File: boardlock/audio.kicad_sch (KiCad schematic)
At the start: 7 parts, among them U4 MAX98357AETE+T

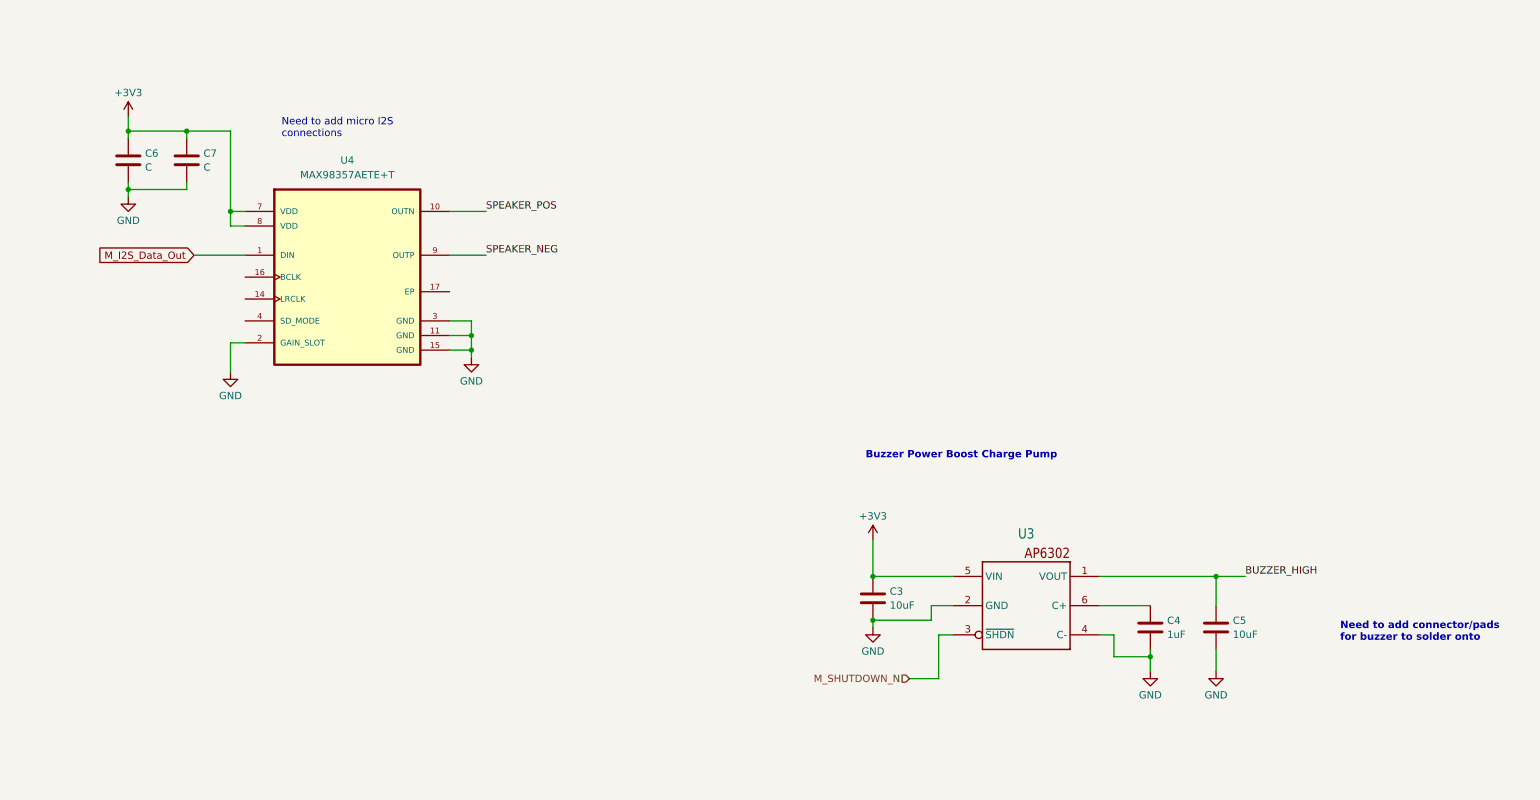
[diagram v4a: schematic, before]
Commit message: added buck boost topology
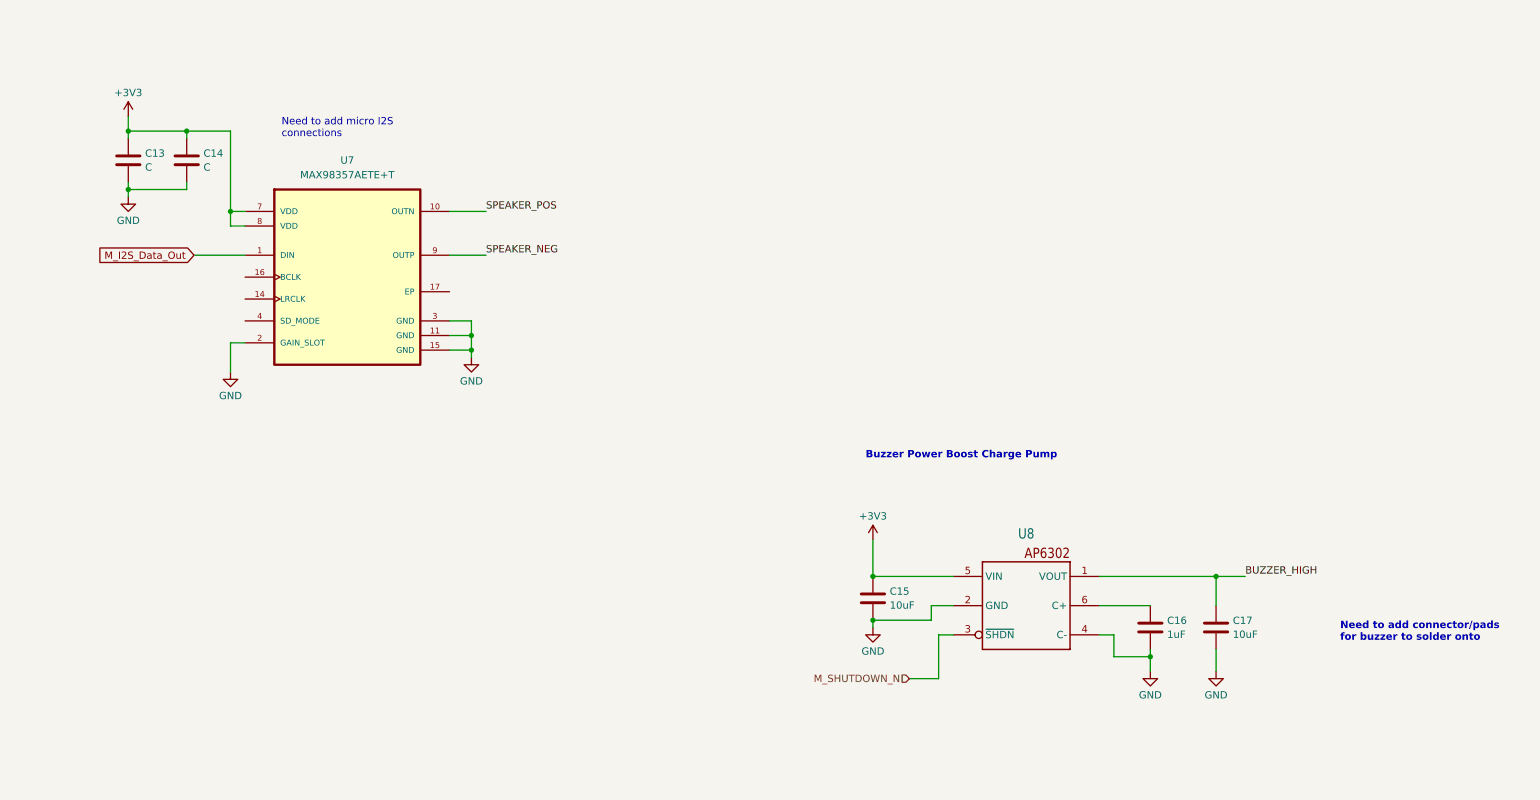
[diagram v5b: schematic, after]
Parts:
- renumbered C6 to C13, C7 to C14, C3 to C15, C4 to C16, C5 to C17, U4 to U7, U3 to U8
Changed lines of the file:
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@@
   (symbol (lib_id "Device:C") (at 231.14 125.73 0) (unit 1)
     (in_bom yes) (on_board yes) (dnp no) (fields_autoplaced)
-    (property "Reference" "C5" (at 234.061 124.5179 0)
+    (property "Reference" "C17" (at 234.061 124.5179 0)
       (effects (font (size 1.27 1.27)) (justify left))
     )
@@
       (project "boardlock"
         (path "/e1fc29ce-837e-4062-84d8-c7e423f9eab9/1eb676fb-9e7a-4e01-ba1e-2eff94d7b66e"
-          (reference "C5") (unit 1)
+          (reference "C17") (unit 1)
         )
       )
@@
   (symbol (lib_id "power:GND") (at 171.45 125.73 0) (unit 1)
     (in_bom yes) (on_board yes) (dnp no) (fields_autoplaced)
-    (property "Reference" "#PWR010" (at 171.45 132.08 0)
+    (property "Reference" "#PWR025" (at 171.45 132.08 0)
       (effects (font (size 1.27 1.27)) hide)
     )
@@
       (project "boardlock"
         (path "/e1fc29ce-837e-4062-84d8-c7e423f9eab9/1eb676fb-9e7a-4e01-ba1e-2eff94d7b66e"
-          (reference "#PWR010") (unit 1)
+          (reference "#PWR025") (unit 1)
         )
       )
@@
   (symbol (lib_id "power:GND") (at 231.14 133.35 0) (unit 1)
     (in_bom yes) (on_board yes) (dnp no) (fields_autoplaced)
-    (property "Reference" "#PWR013" (at 231.14 139.7 0)
+    (property "Reference" "#PWR027" (at 231.14 139.7 0)
       (effects (font (size 1.27 1.27)) hide)
     )
@@
       (project "boardlock"
         (path "/e1fc29ce-837e-4062-84d8-c7e423f9eab9/1eb676fb-9e7a-4e01-ba1e-2eff94d7b66e"
-          (reference "#PWR013") (unit 1)
+          (reference "#PWR027") (unit 1)
         )
       )
@@
   (symbol (lib_id "Device:C") (at 41.91 44.45 0) (unit 1)
     (in_bom yes) (on_board yes) (dnp no) (fields_autoplaced)
-    (property "Reference" "C6" (at 44.831 43.2379 0)
+    (property "Reference" "C13" (at 44.831 43.2379 0)
       (effects (font (size 1.27 1.27)) (justify left))
     )
@@
       (project "boardlock"
         (path "/e1fc29ce-837e-4062-84d8-c7e423f9eab9/1eb676fb-9e7a-4e01-ba1e-2eff94d7b66e"
-          (reference "C6") (unit 1)
+          (reference "C13") (unit 1)
         )
       )
@@
   (symbol (lib_id "Device:C") (at 171.45 120.65 0) (unit 1)
     (in_bom yes) (on_board yes) (dnp no) (fields_autoplaced)
-    (property "Reference" "C3" (at 174.371 119.4379 0)
+    (property "Reference" "C15" (at 174.371 119.4379 0)
       (effects (font (size 1.27 1.27)) (justify left))
     )
@@
       (project "boardlock"
         (path "/e1fc29ce-837e-4062-84d8-c7e423f9eab9/1eb676fb-9e7a-4e01-ba1e-2eff94d7b66e"
-          (reference "C3") (unit 1)
+          (reference "C15") (unit 1)
         )
       )
@@
   (symbol (lib_id "power:GND") (at 219.71 133.35 0) (unit 1)
     (in_bom yes) (on_board yes) (dnp no) (fields_autoplaced)
-    (property "Reference" "#PWR011" (at 219.71 139.7 0)
+    (property "Reference" "#PWR026" (at 219.71 139.7 0)
       (effects (font (size 1.27 1.27)) hide)
     )
@@
       (project "boardlock"
         (path "/e1fc29ce-837e-4062-84d8-c7e423f9eab9/1eb676fb-9e7a-4e01-ba1e-2eff94d7b66e"
-          (reference "#PWR011") (unit 1)
+          (reference "#PWR026") (unit 1)
         )
       )
@@
   (symbol (lib_id "power:+3V3") (at 171.45 110.49 0) (unit 1)
     (in_bom yes) (on_board yes) (dnp no) (fields_autoplaced)
-    (property "Reference" "#PWR012" (at 171.45 114.3 0)
+    (property "Reference" "#PWR024" (at 171.45 114.3 0)
       (effects (font (size 1.27 1.27)) hide)
     )
@@
       (project "boardlock"
         (path "/e1fc29ce-837e-4062-84d8-c7e423f9eab9/1eb676fb-9e7a-4e01-ba1e-2eff94d7b66e"
-          (reference "#PWR012") (unit 1)
+          (reference "#PWR024") (unit 1)
         )
       )
@@
   (symbol (lib_id "power:+3V3") (at 41.91 36.83 0) (unit 1)
     (in_bom yes) (on_board yes) (dnp no) (fields_autoplaced)
-    (property "Reference" "#PWR014" (at 41.91 40.64 0)
+    (property "Reference" "#PWR020" (at 41.91 40.64 0)
       (effects (font (size 1.27 1.27)) hide)
     )
@@
       (project "boardlock"
         (path "/e1fc29ce-837e-4062-84d8-c7e423f9eab9/1eb676fb-9e7a-4e01-ba1e-2eff94d7b66e"
-          (reference "#PWR014") (unit 1)
+          (reference "#PWR020") (unit 1)
         )
       )
@@
   (symbol (lib_id "custom_library:AP3602") (at 198.12 121.92 0) (unit 1)
     (in_bom yes) (on_board yes) (dnp no) (fields_autoplaced)
-    (property "Reference" "U3" (at 198.12 109.4182 0)
+    (property "Reference" "U8" (at 198.12 109.4182 0)
       (effects (font (size 1.778 1.5113)))
     )
@@
       (project "boardlock"
         (path "/e1fc29ce-837e-4062-84d8-c7e423f9eab9/1eb676fb-9e7a-4e01-ba1e-2eff94d7b66e"
-          (reference "U3") (unit 1)
+          (reference "U8") (unit 1)
         )
       )
@@
   (symbol (lib_id "Device:C") (at 219.71 125.73 0) (unit 1)
     (in_bom yes) (on_board yes) (dnp no) (fields_autoplaced)
-    (property "Reference" "C4" (at 222.631 124.5179 0)
+    (property "Reference" "C16" (at 222.631 124.5179 0)
       (effects (font (size 1.27 1.27)) (justify left))
     )
@@
       (project "boardlock"
         (path "/e1fc29ce-837e-4062-84d8-c7e423f9eab9/1eb676fb-9e7a-4e01-ba1e-2eff94d7b66e"
-          (reference "C4") (unit 1)
+          (reference "C16") (unit 1)
         )
       )
@@
   (symbol (lib_id "power:GND") (at 101.6 78.74 0) (unit 1)
     (in_bom yes) (on_board yes) (dnp no) (fields_autoplaced)
-    (property "Reference" "#PWR017" (at 101.6 85.09 0)
+    (property "Reference" "#PWR023" (at 101.6 85.09 0)
       (effects (font (size 1.27 1.27)) hide)
     )
@@
       (project "boardlock"
         (path "/e1fc29ce-837e-4062-84d8-c7e423f9eab9/1eb676fb-9e7a-4e01-ba1e-2eff94d7b66e"
-          (reference "#PWR017") (unit 1)
+          (reference "#PWR023") (unit 1)
         )
       )
@@
   (symbol (lib_id "power:GND") (at 41.91 50.8 0) (unit 1)
     (in_bom yes) (on_board yes) (dnp no) (fields_autoplaced)
-    (property "Reference" "#PWR015" (at 41.91 57.15 0)
+    (property "Reference" "#PWR021" (at 41.91 57.15 0)
       (effects (font (size 1.27 1.27)) hide)
     )
@@
       (project "boardlock"
         (path "/e1fc29ce-837e-4062-84d8-c7e423f9eab9/1eb676fb-9e7a-4e01-ba1e-2eff94d7b66e"
-          (reference "#PWR015") (unit 1)
+          (reference "#PWR021") (unit 1)
         )
       )
@@
   (symbol (lib_id "Device:C") (at 52.07 44.45 0) (unit 1)
     (in_bom yes) (on_board yes) (dnp no) (fields_autoplaced)
-    (property "Reference" "C7" (at 54.991 43.2379 0)
+    (property "Reference" "C14" (at 54.991 43.2379 0)
       (effects (font (size 1.27 1.27)) (justify left))
     )
@@
       (project "boardlock"
         (path "/e1fc29ce-837e-4062-84d8-c7e423f9eab9/1eb676fb-9e7a-4e01-ba1e-2eff94d7b66e"
-          (reference "C7") (unit 1)
+          (reference "C14") (unit 1)
         )
       )
@@
   (symbol (lib_id "MAX98357AETE+T:MAX98357AETE+T") (at 80.01 64.77 0) (unit 1)
     (in_bom yes) (on_board yes) (dnp no) (fields_autoplaced)
-    (property "Reference" "U4" (at 80.01 44.45 0)
+    (property "Reference" "U7" (at 80.01 44.45 0)
       (effects (font (size 1.27 1.27)))
     )
@@
       (project "boardlock"
         (path "/e1fc29ce-837e-4062-84d8-c7e423f9eab9/1eb676fb-9e7a-4e01-ba1e-2eff94d7b66e"
-          (reference "U4") (unit 1)
+          (reference "U7") (unit 1)
         )
       )
@@
   (symbol (lib_id "power:GND") (at 59.69 81.28 0) (unit 1)
     (in_bom yes) (on_board yes) (dnp no) (fields_autoplaced)
-    (property "Reference" "#PWR016" (at 59.69 87.63 0)
+    (property "Reference" "#PWR022" (at 59.69 87.63 0)
       (effects (font (size 1.27 1.27)) hide)
     )
@@
       (project "boardlock"
         (path "/e1fc29ce-837e-4062-84d8-c7e423f9eab9/1eb676fb-9e7a-4e01-ba1e-2eff94d7b66e"
-          (reference "#PWR016") (unit 1)
-        )
-      )
+          (reference "#PWR022") (unit 1)
+        )
+      )

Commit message: modifications?
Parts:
- added J3: Micro_SD_Card_Det1, symbol Connector:Micro_SD_Card_Det1
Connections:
- net +3V3: now also J3.4 (VDD)
- net GND: now also J3.10 (SHIELD), J3.6 (VSS), J3.9 (DET)
- new net M_SPI_CLK: J3.5 (CLK)
- new net M_SPI_CS: J3.2 (DAT3/CD)
- new net M_SPI_MISO: J3.7 (DAT0)
- new net M_SPI_MOSI: J3.3 (CMD)
- no-connect marks 0 -> 2
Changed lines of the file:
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@@
   (junction (at 171.45 124.46) (diameter 0) (color 0 0 0 0)
   )
+  (junction (at 73.66 146.05) (diameter 0) (color 0 0 0 0)
+  )
   (junction (at 59.69 53.34) (diameter 0) (color 0 0 0 0)
   )
@@
   (junction (at 219.71 130.81) (diameter 0) (color 0 0 0 0)
   )
+  (no_connect (at 90.17 140.97))
+  (no_connect (at 90.17 123.19))
+  (wire (pts (xy 73.66 149.86) (xy 73.66 146.05))
+    (stroke (width 0) (type default))
+  )
   (wire (pts (xy 219.71 130.81) (xy 219.71 133.35))
     (stroke (width 0) (type default))
   )
+  (wire (pts (xy 134.62 146.05) (xy 134.62 147.32))
+    (stroke (width 0) (type default))
+  )
   (wire (pts (xy 41.91 39.37) (xy 52.07 39.37))
     (stroke (width 0) (type default))
@@
     (stroke (width 0) (type default))
   )
+  (wire (pts (xy 73.66 146.05) (xy 73.66 135.89))
+    (stroke (width 0) (type default))
+  )
   (wire (pts (xy 59.69 76.2) (xy 59.69 81.28))
     (stroke (width 0) (type default))
   )
+  (wire (pts (xy 88.9 125.73) (xy 90.17 125.73))
+    (stroke (width 0) (type default))
+  )
   (wire (pts (xy 59.69 76.2) (xy 62.23 76.2))
     (stroke (width 0) (type default))
@@
     (stroke (width 0) (type default))
   )
+  (wire (pts (xy 90.17 133.35) (xy 88.9 133.35))
+    (stroke (width 0) (type default))
+  )
   (wire (pts (xy 41.91 36.83) (xy 41.91 39.37))
     (stroke (width 0) (type default))
@@
     (stroke (width 0) (type default))
   )
+  (wire (pts (xy 73.66 146.05) (xy 90.17 146.05))
+    (stroke (width 0) (type default))
+  )
   (wire (pts (xy 181.61 121.92) (xy 185.42 121.92))
     (stroke (width 0) (type default))
@@
     (stroke (width 0) (type default))
   )
+  (wire (pts (xy 73.66 135.89) (xy 90.17 135.89))
+    (stroke (width 0) (type default))
+  )
+  (wire (pts (xy 90.17 128.27) (xy 88.9 128.27))
+    (stroke (width 0) (type default))
+  )
   (wire (pts (xy 97.79 77.47) (xy 101.6 77.47))
     (stroke (width 0) (type default))
@@
     (stroke (width 0) (type default))
   )
+  (wire (pts (xy 134.62 146.05) (xy 133.35 146.05))
+    (stroke (width 0) (type default))
+  )
   (wire (pts (xy 59.69 53.34) (xy 59.69 55.88))
     (stroke (width 0) (type default))
@@
     (stroke (width 0) (type default))
   )
+  (wire (pts (xy 90.17 138.43) (xy 88.9 138.43))
+    (stroke (width 0) (type default))
+  )
   (wire (pts (xy 219.71 130.81) (xy 219.71 129.54))
     (stroke (width 0) (type default))
@@
     (stroke (width 0) (type default))
   )
+  (wire (pts (xy 73.66 120.65) (xy 73.66 130.81))
+    (stroke (width 0) (type default))
+  )
   (wire (pts (xy 101.6 74.93) (xy 101.6 77.47))
     (stroke (width 0) (type default))
@@
   )
   (wire (pts (xy 97.79 60.96) (xy 104.14 60.96))
+    (stroke (width 0) (type default))
+  )
+  (wire (pts (xy 73.66 130.81) (xy 90.17 130.81))
     (stroke (width 0) (type default))
   )
@@
     (effects (font (size 1.27 1.27)) (justify left bottom))
   )
+  (global_label "M_SPI_CLK" (shape input) (at 88.9 133.35 180) (fields_autoplaced)
+    (effects (font (size 1.27 1.27)) (justify right))
+    (property "Intersheetrefs" "${INTERSHEET_REFS}" (at 75.9552 133.35 0)
+      (effects (font (size 1.27 1.27)) (justify right) hide)
+    )
+  )
+  (global_label "M_SPI_MISO" (shape output) (at 88.9 138.43 180) (fields_autoplaced)
+    (effects (font (size 1.27 1.27)) (justify right))
+    (property "Intersheetrefs" "${INTERSHEET_REFS}" (at 74.9271 138.43 0)
+      (effects (font (size 1.27 1.27)) (justify right) hide)
+    )
+  )
+  (global_label "M_SPI_CS" (shape input) (at 88.9 125.73 180) (fields_autoplaced)
+    (effects (font (size 1.27 1.27)) (justify right))
+    (property "Intersheetrefs" "${INTERSHEET_REFS}" (at 77.0438 125.73 0)
+      (effects (font (size 1.27 1.27)) (justify right) hide)
+    )
+  )
   (global_label "M_I2S_Data_Out" (shape input) (at 53.34 60.96 180) (fields_autoplaced)
     (effects (font (size 1.27 1.27)) (justify right))
@@
     )
   )
+  (global_label "M_SPI_MOSI" (shape input) (at 88.9 128.27 180) (fields_autoplaced)
+    (effects (font (size 1.27 1.27)) (justify right))
+    (property "Intersheetrefs" "${INTERSHEET_REFS}" (at 74.9271 128.27 0)
+      (effects (font (size 1.27 1.27)) (justify right) hide)
+    )
+  )
   (hierarchical_label "M_SHUTDOWN_N" (shape input) (at 177.8 134.62 180) (fields_autoplaced)
     (effects (font (size 1.27 1.27)) (justify right))
@@
     )
   )
+  (symbol (lib_id "Connector:Micro_SD_Card_Det1") (at 113.03 133.35 0) (unit 1)
+    (in_bom yes) (on_board yes) (dnp no) (fields_autoplaced)
+    (property "Reference" "J3" (at 113.665 113.03 0)
+      (effects (font (size 1.27 1.27)))
+    )
+    (property "Value" "Micro_SD_Card_Det1" (at 113.665 115.57 0)
+      (effects (font (size 1.27 1.27)))
+    )
+    (property "Footprint" "" (at 165.1 115.57 0)
+      (effects (font (size 1.27 1.27)) hide)
+    )
+    (property "Datasheet" "https://datasheet.lcsc.com/lcsc/2110151630_XKB-Connectivity-XKTF-015-N_C381082.pdf" (at 113.03 130.81 0)
+      (effects (font (size 1.27 1.27)) hide)
+    )
+    (pin "1")
+    (pin "10")
+    (pin "2")
+    (pin "3")
+    (pin "4")
+    (pin "5")
+    (pin "6")
+    (pin "7")
+    (pin "8")
+    (pin "9")
+    (instances
+      (project "boardlock"
+        (path "/e1fc29ce-837e-4062-84d8-c7e423f9eab9/1eb676fb-9e7a-4e01-ba1e-2eff94d7b66e"
+          (reference "J3") (unit 1)
+        )
+      )
+    )
+  )
+  (symbol (lib_id "power:GND") (at 73.66 149.86 0) (unit 1)
+    (in_bom yes) (on_board yes) (dnp no)
+    (property "Reference" "#PWR08" (at 73.66 156.21 0)
+      (effects (font (size 1.27 1.27)) hide)
+    )
+    (property "Value" "GND" (at 69.85 151.13 0)
+      (effects (font (size 1.27 1.27)))
+    )
+    (property "Footprint" "" (at 73.66 149.86 0)
+      (effects (font (size 1.27 1.27)) hide)
+    )
+    (property "Datasheet" "" (at 73.66 149.86 0)
+      (effects (font (size 1.27 1.27)) hide)
+    )
+    (pin "1")
+    (instances
+      (project "boardlock"
+        (path "/e1fc29ce-837e-4062-84d8-c7e423f9eab9/1eb676fb-9e7a-4e01-ba1e-2eff94d7b66e"
+          (reference "#PWR08") (unit 1)
+        )
+      )
+    )
+  )
   (symbol (lib_id "Device:C") (at 41.91 44.45 0) (unit 1)
     (in_bom yes) (on_board yes) (dnp no) (fields_autoplaced)
@@
         )
       )
+    )
+  )
+  (symbol (lib_id "power:GND") (at 134.62 147.32 0) (unit 1)
+    (in_bom yes) (on_board yes) (dnp no) (fields_autoplaced)
+    (property "Reference" "#PWR050" (at 134.62 153.67 0)
+      (effects (font (size 1.27 1.27)) hide)
+    )
+    (property "Value" "GND" (at 134.62 152.4 0)
+      (effects (font (size 1.27 1.27)))
+    )
+    (property "Footprint" "" (at 134.62 147.32 0)
+      (effects (font (size 1.27 1.27)) hide)
+    )
+    (property "Datasheet" "" (at 134.62 147.32 0)
+      (effects (font (size 1.27 1.27)) hide)
+    )
+    (pin "1")
+    (instances
+      (project "boardlock"
+        (path "/e1fc29ce-837e-4062-84d8-c7e423f9eab9/1eb676fb-9e7a-4e01-ba1e-2eff94d7b66e"
+          (reference "#PWR050") (unit 1)
+        )
+      )
+    )
+  )
+  (symbol (lib_id "power:+3V3") (at 73.66 120.65 0) (unit 1)
+    (in_bom yes) (on_board yes) (dnp no)
+    (property "Reference" "#PWR049" (at 73.66 124.46 0)
+      (effects (font (size 1.27 1.27)) hide)
+    )
+    (property "Value" "+3V3" (at 69.85 120.65 0)
+      (effects (font (size 1.27 1.27)))
+    )
+    (property "Footprint" "" (at 73.66 120.65 0)
+      (effects (font (size 1.27 1.27)) hide)
+    )
+    (property "Datasheet" "" (at 73.66 120.65 0)
+      (effects (font (size 1.27 1.27)) hide)
+    )
+    (pin "1")
+    (instances
+      (project "boardlock"
+        (path "/e1fc29ce-837e-4062-84d8-c7e423f9eab9/1eb676fb-9e7a-4e01-ba1e-2eff94d7b66e"
+          (reference "#PWR049") (unit 1)
+        )
+      )

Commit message: More zecong edits
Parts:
- added C? (x2): 10uF, symbol Device:C
- added D?: PMEG2005EH, Diode_SMD:D_SOD-123F, symbol Diode:PMEG2005EH
- added J?: Conn_01x02, Connector_JST:JST_XA_B02B-XASK-1-A_1x02_P2.50mm_Vertical, symbol Connector_Generic:Conn_01x02
- added L?: 4.7uH, symbol Device:L
- added R?: 1.05M, symbol Device:R_US
- added R?: 120k, symbol Device:R_US
- added U?: MCP1661, Package_TO_SOT_SMD:SOT-23-5, symbol Driver_LED:MCP1662-xOT
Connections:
- net +3V3: now also C?.1, L?.1, U?.5 (V_{IN})
- net GND: now also U7.17 (EP), C?.2, C?.2, R?.2, U?.2 (GND)
- net SPEAKER_NEG: now also J?.2 (Pin_2)
- net SPEAKER_POS: now also J?.1 (Pin_1)
- net M_I2S_LRC: now reaches U7.14 (LRCLK)
- net M_I2S_BCLK: now reaches U7.16 (BCLK)
- net BUZZER_HIGH renamed +5V
- new net: R?.1, R?.2, U?.3 (V_{FB})
- new net: D?.2 (A), L?.2, U?.1 (SW)
- new net +12V: C?.1, D?.1 (K), R?.1
- new net M_BOOST_EN: U?.4 (EN)
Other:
- note added: "12V Boost Converter"
- note added: "5V Charge Pump"
- note added: "Check breakout board for how SD_mode is wired"
- note added: "Dgital Audio Amplifier"
- note added: "Keeping Charge Pump Here Just in Case we need to use it. Unlikley with the boost converter present."
- note added: "NOTE: Repurposed MCP1662 Symbol"
- note added: "Need to update Gain Slot as I test new speakers"
- note added: "V_FB = 1.227V"
- company: (none) -> Schetmatic
- title: (none) -> BoardLock Schematic
- moved on the sheet: C15, C16, C17, J3, U8
